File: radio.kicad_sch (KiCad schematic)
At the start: 87 parts, among them CN15 DF40C-20DP-0.4V, J19 SUBGHZ SMA, J20 GPS SMA, Q1 NPN, SW3 4*4*1.7, U18 RP2350B, U19 TXM27.12M0004322DBBDO00T, U20 CC1101RGPR, U21 0896BM15A0001001E, U23 EM4095HMSO16B+, U24 PE4259-63, U25 PE4259-63, U26 PE4259-63, U27 PE4259-63, U28 0433BM15A0001001E, U29 PN7160A1HN/C100Y, U31 S2B-PH-K-S-GW, U32 S2B-PH-K-S-GW, U33 W25Q128JVSIQTR, U34 SiP32508DT, U35 SiP32508DT, Y1 12MHz, Y3 26.0MHz

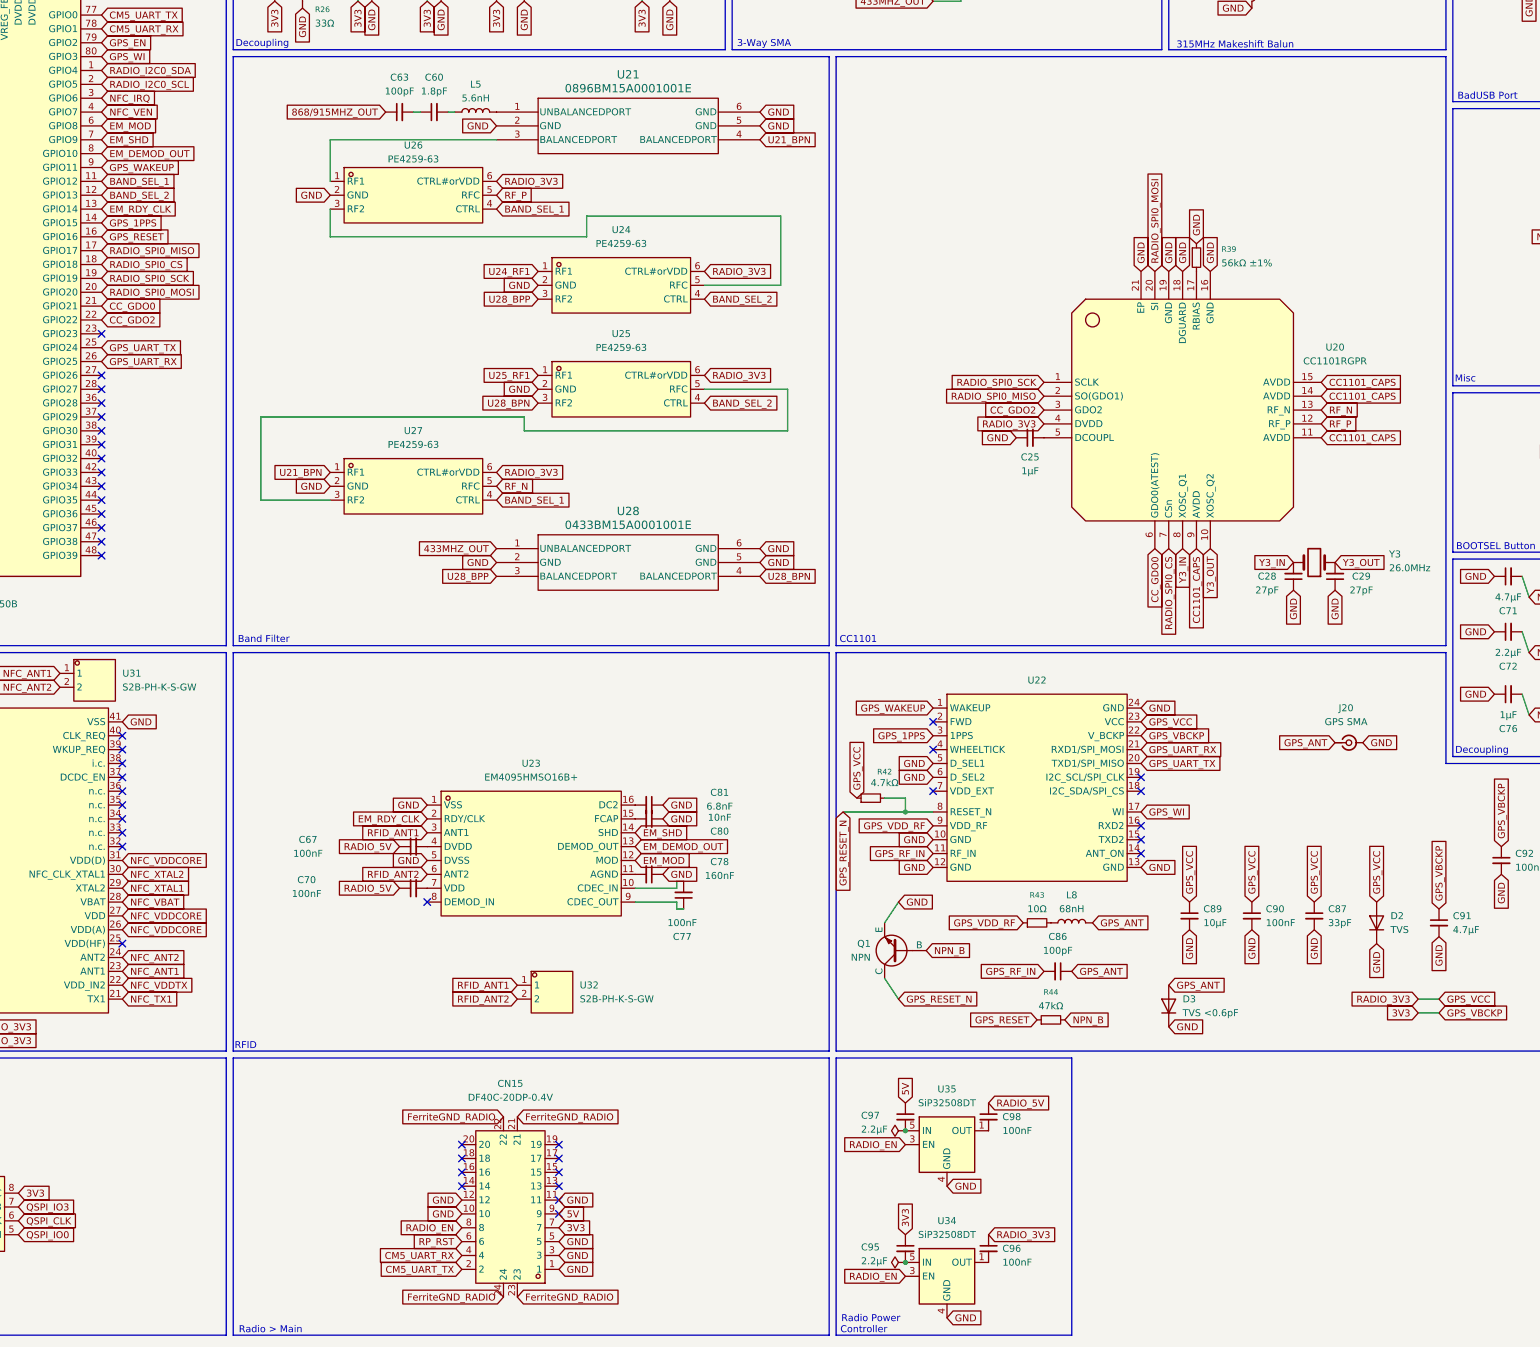
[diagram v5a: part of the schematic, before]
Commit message: finished slateconnect i2c gpio expander, completed led status bar schematic, fixed all drc errors, started assigning footprints and started bom
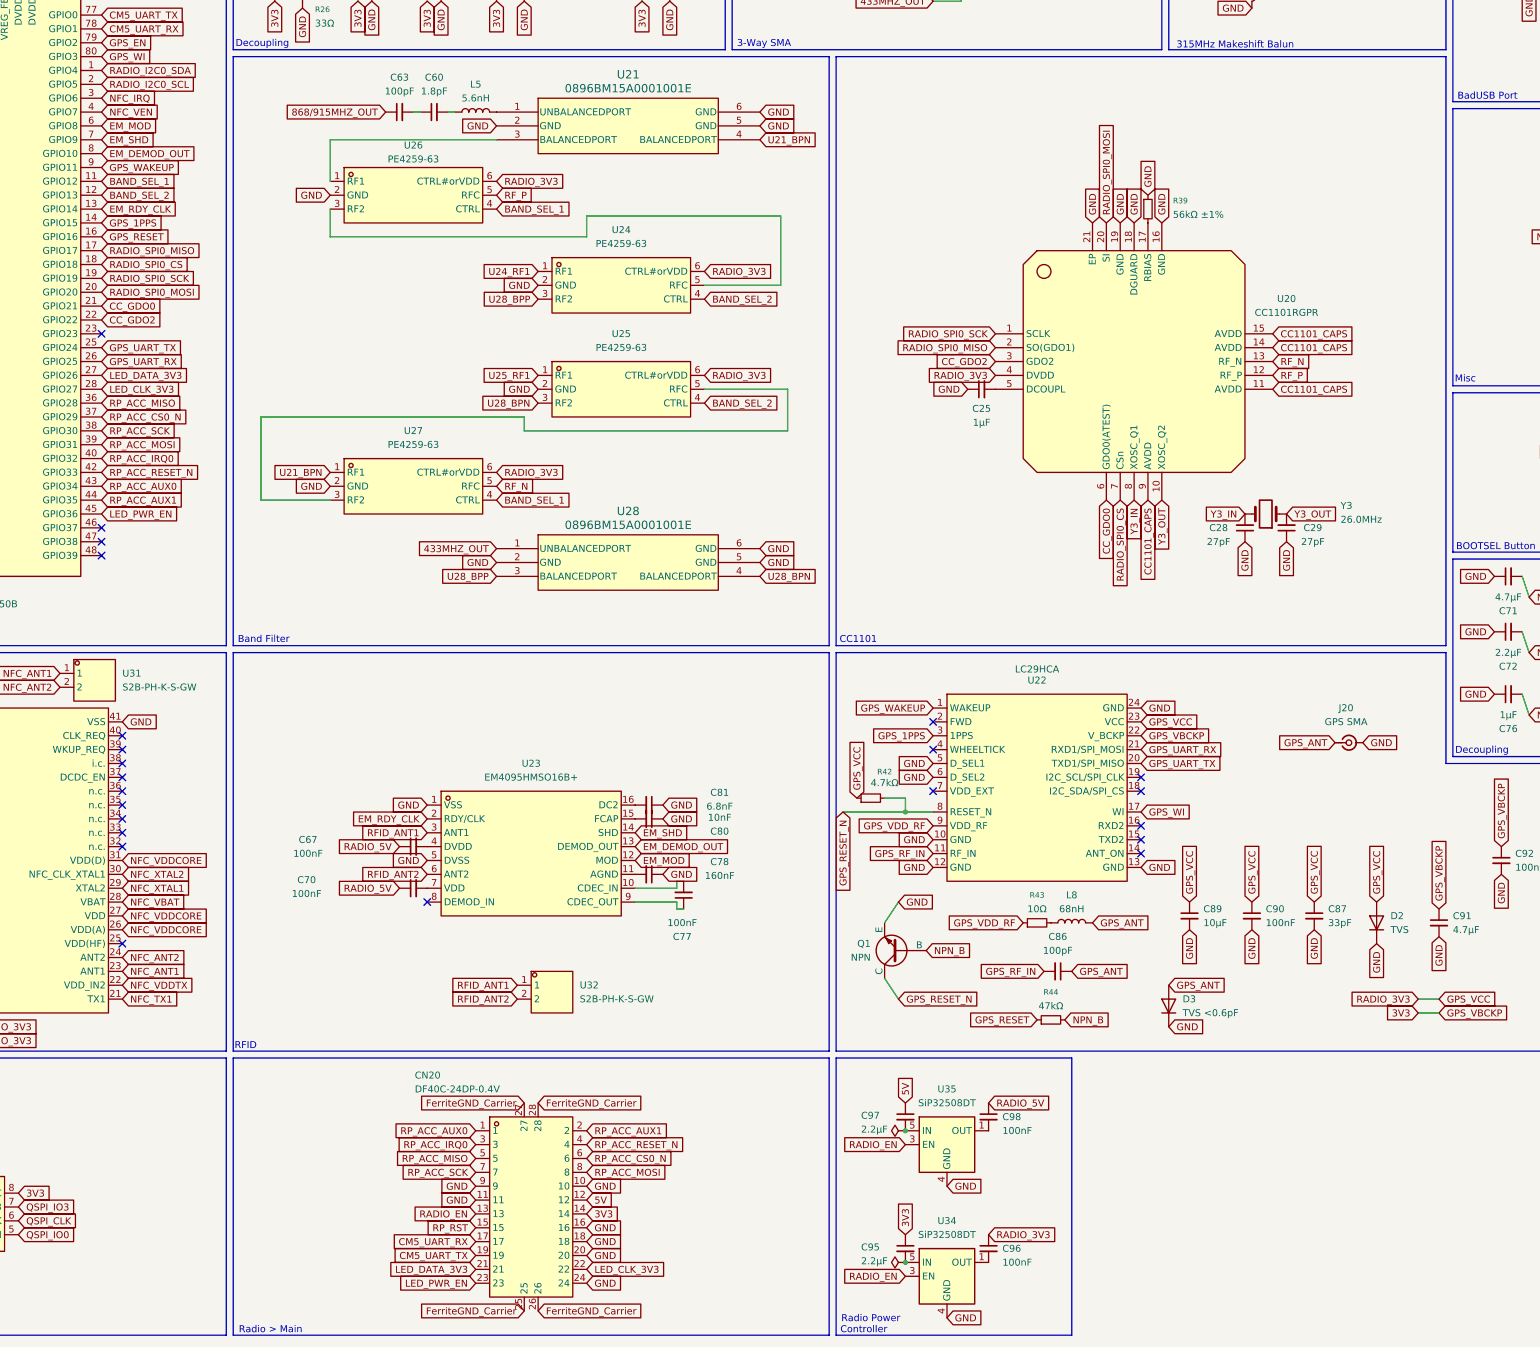
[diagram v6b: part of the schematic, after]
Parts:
- removed CN15: DF40C-20DP-0.4V, slate113:CONN-SMD_20P-P0.40_HRS_DF40TC-20DP-0.4V, symbol slate113:DF40C-20DP-0.4V
- added CN20: DF40C-24DP-0.4V, slate113:CONN-SMD_DF40C-24DP-0.4V, symbol slate113:DF40C-24DP-0.4V
- C25: footprint (none) -> Capacitor_SMD:C_0603_1608Metric; MPN (none) -> CL10B105KA8NNNC; Manufacturer (none) -> Samsung Electro-Mechanics
- C58, C59, C69, C70, C92, C96, C98: footprint (none) -> Capacitor_SMD:C_0603_1608Metric; MPN (none) -> CL10B104KB8NNNC; Manufacturer (none) -> Samsung Electro-Mechanics
- C63: footprint (none) -> Capacitor_SMD:C_0603_1608Metric; MPN (none) -> CL10C101JB8NNNC; Manufacturer (none) -> Samsung Electro-Mechanics
- C64: footprint (none) -> Capacitor_SMD:C_0603_1608Metric; MPN (none) -> CL10C689JB8NNNC; Manufacturer (none) -> Samsung Electro-Mechanics
- C75, C79: footprint (none) -> Capacitor_SMD:C_0603_1608Metric; MPN (none) -> CL10B225KA8NNNC; Manufacturer (none) -> Samsung Electro-Mechanics
- C82, C83, C85: footprint (none) -> Capacitor_SMD:C_0603_1608Metric; MPN (none) -> CL10B475KA8NNNC; Manufacturer (none) -> Samsung Electro-Mechanics
- C89: footprint (none) -> Capacitor_SMD:C_0603_1608Metric; MPN (none) -> CL10A106KP8NNNC; Manufacturer (none) -> Samsung Electro-Mechanics
- D2, D4: MPN (none) -> Nexperia PESD3V3U1UL; Manufacturer (none) -> DigiKey
- D3: MPN (none) -> TVS <0.6pF; Manufacturer (none) -> LCSC
- R38: footprint (none) -> Resistor_SMD:R_0603_1608Metric; MPN (none) -> RC0603FR-0710KL; Manufacturer (none) -> Yageo
- U18: MPN (none) -> RP2350B; Manufacturer (none) -> LCSC
- U21: MPN (none) -> 0896BM15A0001001E; Manufacturer (none) -> LCSC
- U22: value (none) -> LC29HCA; MPN (none) -> Quectel LC29HCA; Manufacturer (none) -> Quectel
- U28: value 0433BM15A0001001E -> 0896BM15A0001001E; MPN (none) -> 0896BM15A0001001E; Manufacturer (none) -> LCSC
- U34, U35: MPN (none) -> SiP32508DT; Manufacturer (none) -> LCSC
- Y1: MPN (none) -> Abracon ABM8G-12.000MHZ-18-D2Y-T; Manufacturer (none) -> DigiKey
- Y3: MPN (none) -> Abracon ABM8G-26.000MHZ-18-D2Y-T; Manufacturer (none) -> DigiKey
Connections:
- net 3V3: now also CN20.14
- net 5V: now also CN20.12
- net CM5_UART_RX: now also CN20.17
- net CM5_UART_TX: now also CN20.19
- net GND: now also CN20.10, CN20.11, CN20.16, CN20.18, CN20.20, CN20.24, CN20.9
- net RADIO_EN: now also CN20.13
- net RP_RST: now also CN20.15
- net LED_DATA_3V3: now reaches U18.27 (GPIO26)
- net LED_DATA_3V3: now also CN20.21
- net LED_CLK_3V3: now reaches U18.28 (GPIO27)
- net LED_CLK_3V3: now also CN20.22
- net RP_ACC_MISO: now reaches U18.36 (GPIO28)
- net RP_ACC_MISO: now also CN20.5
- net RP_ACC_CS0_N: now reaches U18.37 (GPIO29)
- net RP_ACC_CS0_N: now also CN20.6
- net RP_ACC_SCK: now reaches U18.38 (GPIO30)
- net RP_ACC_SCK: now also CN20.7
- net RP_ACC_MOSI: now reaches U18.39 (GPIO31)
- net RP_ACC_MOSI: now also CN20.8
- net RP_ACC_IRQ0: now reaches U18.40 (GPIO32)
- net RP_ACC_IRQ0: now also CN20.3
- net RP_ACC_RESET_N: now reaches U18.42 (GPIO33)
- net RP_ACC_RESET_N: now also CN20.4
- net RP_ACC_AUX0: now reaches U18.43 (GPIO34)
- net RP_ACC_AUX0: now also CN20.1
- net RP_ACC_AUX1: now reaches U18.44 (GPIO35)
- net RP_ACC_AUX1: now also CN20.2
- net LED_PWR_EN: now reaches U18.45 (GPIO36)
- net LED_PWR_EN: now also CN20.23
- new net FerriteGND_Carrier: CN20.25, CN20.26, CN20.27, CN20.28
- no-connect marks 59 -> 38
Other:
- moved on the sheet: C25, C28, C29, R39, U20, Y3

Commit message: finished BOM, replaced discontinued parts, added missing footprints, updated schematics and libraries
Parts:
- C25: LCSC Part (none) -> C15849; MPN CL10B105KA8NNNC -> CL10A105KB8NNNC
- C28, C29: footprint (none) -> Capacitor_SMD:C_0402_1005Metric; LCSC Part (none) -> C1557; MPN (none) -> 0402CG270J500NT
- C35, C66: footprint (none) -> Capacitor_SMD:C_0402_1005Metric; LCSC Part (none) -> C1554; MPN (none) -> 0402CG200J500NT
- C57, C61, C62, C67, C73, C77, C90: footprint (none) -> Capacitor_SMD:C_0603_1608Metric; LCSC Part (none) -> C1591; MPN (none) -> CL10B104KB8NNNC
- C58, C59, C69, C70, C92, C96, C98: LCSC Part (none) -> C1591
- C60: footprint (none) -> Capacitor_SMD:C_0402_1005Metric; LCSC Part (none) -> C258489; MPN (none) -> C1005NPO189CGT
- C63: LCSC Part (none) -> C14858
- C64: footprint Capacitor_SMD:C_0603_1608Metric -> Capacitor_SMD:C_0402_1005Metric; LCSC Part (none) -> C1576; MPN CL10C689JB8NNNC -> 0402CG6R8C500NT
- C65: footprint (none) -> Capacitor_SMD:C_0402_1005Metric; LCSC Part (none) -> C1576; MPN (none) -> 0402CG6R8C500NT
- C68, C71, C84, C91: footprint (none) -> Capacitor_SMD:C_0603_1608Metric; LCSC Part (none) -> C19666; MPN (none) -> CL10A475KO8NNNC
- C72, C74, C95, C97: footprint (none) -> Capacitor_SMD:C_0603_1608Metric; LCSC Part (none) -> C23630; MPN (none) -> CL10A225KO8NNNC
- C75, C79: LCSC Part (none) -> C23630; MPN CL10B225KA8NNNC -> CL10A225KO8NNNC
- C76: footprint (none) -> Capacitor_SMD:C_0603_1608Metric; LCSC Part (none) -> C15849; MPN (none) -> CL10A105KB8NNNC
- C78: value 160nF -> 100nF; footprint (none) -> Capacitor_SMD:C_0603_1608Metric; LCSC Part (none) -> C1591; MPN (none) -> CL10B104KB8NNNC
- C80: footprint (none) -> Capacitor_SMD:C_0603_1608Metric; LCSC Part (none) -> C49326600; MPN (none) -> 0603X7R103J500NT
- C81: footprint (none) -> Capacitor_SMD:C_0603_1608Metric; LCSC Part (none) -> C107097; MPN (none) -> CC0603KRX7R9BB682
- C82, C83, C85: LCSC Part (none) -> C19666; MPN CL10B475KA8NNNC -> CL10A475KO8NNNC
- C86: footprint (none) -> Capacitor_SMD:C_0603_1608Metric; LCSC Part (none) -> C14858; MPN (none) -> CL10C101JB8NNNC
- C87, C88: footprint (none) -> Capacitor_SMD:C_0603_1608Metric; LCSC Part (none) -> C1663; MPN (none) -> CL10C330JB8NNNC
- C89: LCSC Part (none) -> C380317; MPN CL10A106KP8NNNC -> TCC0603X5R106M160CT
- D2, D4: DigiKey Part (none) -> 1727-4154-2-ND; LCSC Part (none) -> C19829543; MPN Nexperia PESD3V3U1UL -> PESD3V3U1UL
- D3: value TVS <0.6pF -> RCLAMP0521PATCT; DigiKey Part (none) -> RCLAMP0521PATR-ND; MPN TVS <0.6pF -> RCLAMP0521PATCT; Manufacturer LCSC -> Semtech
- FB4: LCSC Part (none) -> C80165; MPN (none) -> BLM18PG221SN1D; Manufacturer (none) -> Murata Electronics
- FB5: LCSC Part (none) -> C107335; MPN (none) -> MPZ1608S601ATA00; Manufacturer (none) -> TDK
- J19: value SUBGHZ SMA -> U.FL; footprint (none) -> slate113:IPEX-SMD_BWIPX-1-001E; LCSC Part (none) -> C496552; MPN (none) -> BWIPX-1-001E
- J20: value GPS SMA -> U.FL; footprint (none) -> slate113:IPEX-SMD_BWIPX-1-001E; LCSC Part (none) -> C496552; MPN (none) -> BWIPX-1-001E
- L5: footprint (none) -> Inductor_SMD:L_0402_1005Metric; LCSC Part (none) -> C85670; MPN (none) -> LQG15HS5N6S02D
- L6, L7: footprint (none) -> Inductor_SMD:L_0402_1005Metric; LCSC Part (none) -> C113114; MPN (none) -> LQW15AN33NG00D
- L8: footprint (none) -> Inductor_SMD:L_0402_1005Metric; LCSC Part (none) -> C108965; MPN (none) -> LQW15AN68NG00D
- Q1: LCSC Part (none) -> C77991; MPN (none) -> MMBT3904-TP; Manufacturer (none) -> MCC (Micro Commercial Components)
- R26: footprint (none) -> Resistor_SMD:R_0603_1608Metric; LCSC Part (none) -> C23140; MPN (none) -> 0603WAF330JT5E
- R38: LCSC Part (none) -> C25804; MPN RC0603FR-0710KL -> 0603WAF1002T5E
- R39: footprint (none) -> Resistor_SMD:R_0603_1608Metric; LCSC Part (none) -> C23206; MPN (none) -> 0603WAF5602T5E
- R40, R41: footprint (none) -> Resistor_SMD:R_0603_1608Metric; LCSC Part (none) -> C23186; MPN (none) -> 0603WAF5101T5E
- R42: footprint (none) -> Resistor_SMD:R_0603_1608Metric; LCSC Part (none) -> C23162; MPN (none) -> 0603WAF4701T5E
- R43: footprint (none) -> Resistor_SMD:R_0603_1608Metric; LCSC Part (none) -> C22859; MPN (none) -> 0603WAF100JT5E
- R44: footprint (none) -> Resistor_SMD:R_0603_1608Metric; LCSC Part (none) -> C25819; MPN (none) -> 0603WAF4702T5E
- U18: value RP2350B -> ESP32-S3-WROOM-1U-N8; footprint Package_DFN_QFN:QFN-80-1EP_10x10mm_P0.4mm_EP3.4x3.4mm -> (none); LCSC Part (none) -> C2980297; MPN RP2350B -> ESP32-S3-WROOM-1U-N8; Manufacturer LCSC -> Espressif Systems
- U21, U28: LCSC Part (none) -> C2917678
- U22: value LC29HCA -> LC29HBA; footprint (none) -> slate113:LC29H; DigiKey Part (none) -> 2958-LC29HBAMDTR-ND; MPN Quectel LC29HCA -> LC29HBAMD
- U34, U35: LCSC Part (none) -> C139515; MPN SiP32508DT -> SIP32508DT-T1-GE3
- Y1: footprint (none) -> slate113:CRYSTAL-SMD_4P-L3.2-W2.5-BL; LCSC Part (none) -> C70565; MPN Abracon ABM8G-12.000MHZ-18-D2Y-T -> X322512MOB4SI
- Y3: footprint (none) -> slate113:CRYSTAL-SMD_4P-L3.2-W2.5-BL; LCSC Part (none) -> C15192; MPN Abracon ABM8G-26.000MHZ-18-D2Y-T -> X322526MMB4SI
